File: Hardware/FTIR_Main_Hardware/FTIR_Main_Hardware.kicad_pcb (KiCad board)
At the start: 2 copper layers, 63 parts, among them J1 RJ45_LED_Shielded, Q1 IRF7606PBF, Q2 BSS138, Q3 IRF7606PBF, Q4 IRF7606PBF, Q5 BSS138, Q6 BSS138, U1 Opamp_Dual, U2 D36V28F7, U3 OKI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

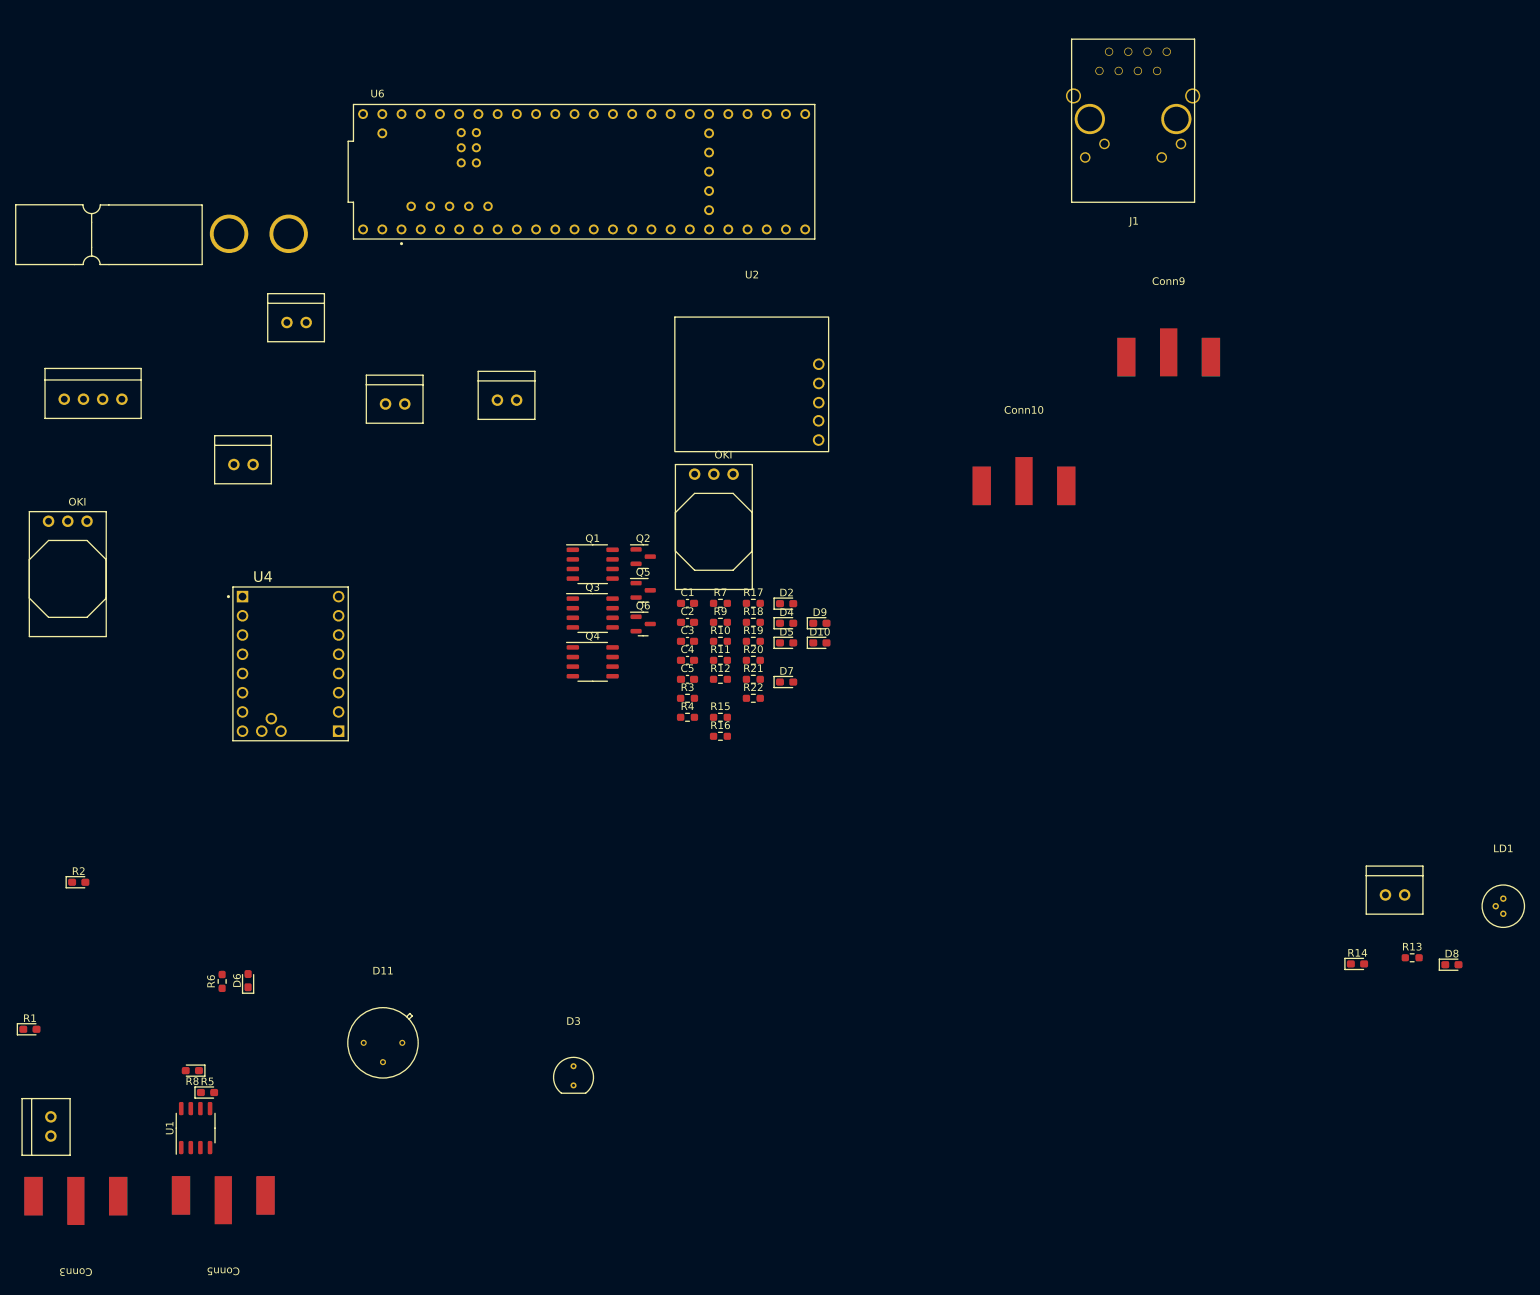
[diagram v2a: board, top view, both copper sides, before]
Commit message: Fixed all custom footprint problems and began boards
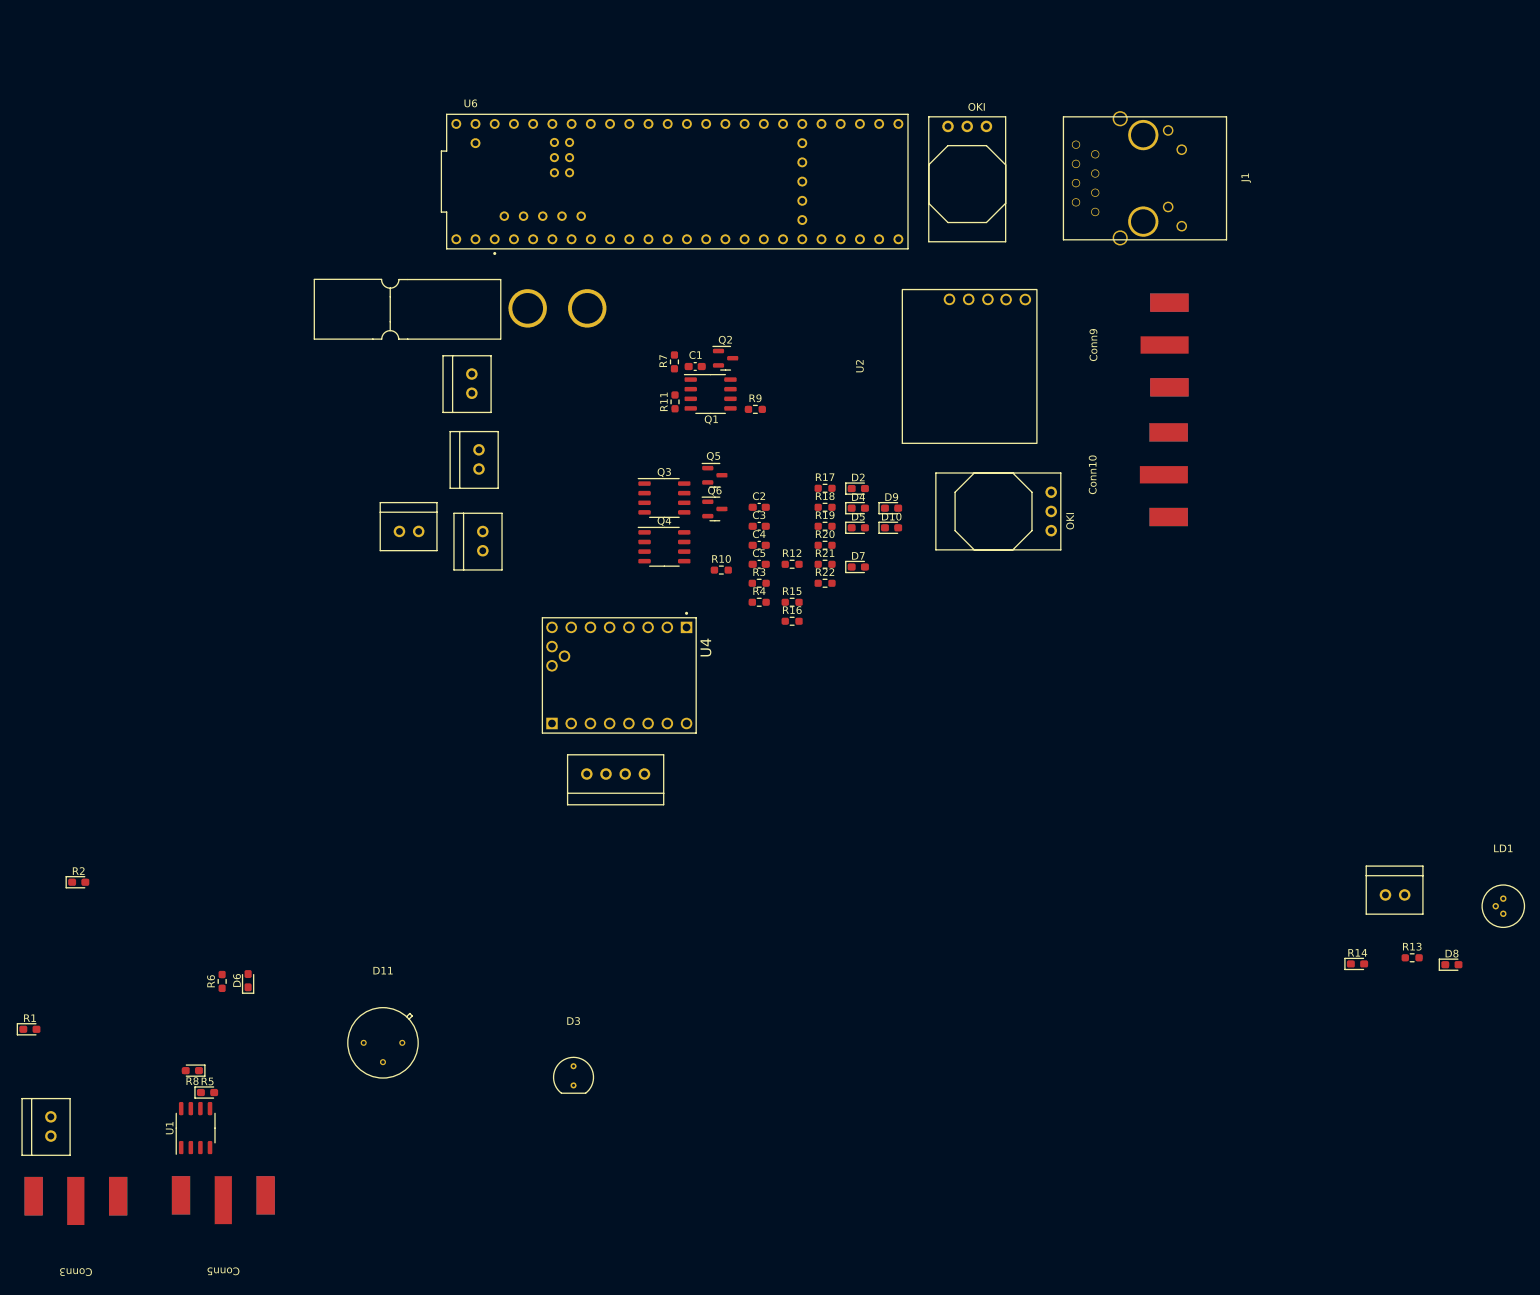
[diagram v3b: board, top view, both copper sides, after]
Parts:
- moved U7 132.5 mm to (194.5, 83.2), turned to -90 degrees
- moved Conn4 91.3 mm to (140.7, 120.5), turned to 180 degrees
- moved U3 56.9 mm to (180.8, 34.9)
- moved U4 43.9 mm to (137.4, 106.9), turned to -90 degrees
- moved Conn1 40.7 mm to (125.3, 58.9)
- moved Conn11 34.8 mm to (119.4, 91.0), turned to 90 degrees
- moved R11 34.7 mm to (144.8, 71.3), turned to 90 degrees
- moved R7 32.5 mm to (144.7, 66.0), turned to -90 degrees
- moved C1 31.3 mm to (147.4, 66.6)
- moved R9 28.5 mm to (155.4, 72.3)
- moved Q2 28.4 mm to (151.5, 65.5)
- moved Q1 27.4 mm to (149.5, 70.3)
- moved Conn6 26.2 mm to (117.9, 70.2), turned to 90 degrees
- moved U2 25.3 mm to (180.3, 66.5), turned to 90 degrees
- moved Conn10 19.2 mm to (210.0, 80.9), turned to 90 degrees
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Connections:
- Conn1 pad 4: (no net) -> +12V
- U2 pad EN: (no net) -> BUCK_EN
- U2 pad GND: (no net) -> GND
- U2 pad VIN: (no net) -> +12V
- U2 pad VOUT: (no net) -> +7.5V
- U4 pad CLK: unconnected-(U4-PadCLK) -> CLK
- U4 pad PDN: unconnected-(U4-PadPDN) -> PDN
- U4 pad UART: GND -> UART
- U6 pad 28: unconnected-(U6-RX7-Pad28) -> CLK
- U6 pad 39: unconnected-(U6-A15-Pad39) -> UART
- U6 pad 40: unconnected-(U6-A16-Pad40) -> PDN

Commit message: Rev1 layout ready for review
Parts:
- added H1: MountingHole, MRDT_Drill_Holes:4_40_Hole_Corner, F.Cu at (108.9, 77.0)
- added H10: MountingHole, MRDT_Drill_Holes:4_40_Hole_Corner, F.Cu at (124.7, 112.1)
- added H11: MountingHole, MRDT_Drill_Holes:4_40_Hole_Corner, F.Cu at (142.1, 94.7)
- added H12: MountingHole, MRDT_Drill_Holes:4_40_Hole_Corner, F.Cu at (142.1, 112.1)
- added H2: MountingHole, MRDT_Drill_Holes:4_40_Hole_Corner, F.Cu at (198.7, 77.0)
- added H3: MountingHole, MRDT_Drill_Holes:4_40_Hole_Corner, F.Cu at (108.9, 37.3)
- added H4: MountingHole, MRDT_Drill_Holes:4_40_Hole_Corner, F.Cu at (198.7, 37.3)
- added H5: MountingHole, MRDT_Drill_Holes:4_40_Hole_Corner, F.Cu at (159.4, 97.1)
- added H6: MountingHole, MRDT_Drill_Holes:4_40_Hole_Corner, F.Cu at (169.4, 94.7)
- added H7: MountingHole, MRDT_Drill_Holes:4_40_Hole_Corner, F.Cu at (124.6, 94.6)
- added H8: MountingHole, MRDT_Drill_Holes:4_40_Hole_Corner, F.Cu at (159.3, 94.7)
- added H9: MountingHole, MRDT_Drill_Holes:4_40_Hole_Corner, F.Cu at (169.4, 97.1)
- Conn1: footprint MRDT_Connectors:Anderson_2_Horizontal_Stacked -> MRDT_Connectors:Square_Anderson_2_H_Stacked
- D11, D3, LD1: moved to B.Cu
- moved D8 101.6 mm to (162.8, 89.5)
- moved LD1 99.2 mm to (164.4, 95.9), turned to 180 degrees
- moved Conn5 95.8 mm to (147.4, 103.4), turned to 90 degrees
- moved R13 93.6 mm to (166.6, 89.5), turned to 180 degrees
- moved U1 92.8 mm to (133.1, 90.2), turned to 0 degrees
- moved R1 92.7 mm to (127.6, 91.2), turned to 180 degrees
- moved R8 91.1 mm to (138.7, 89.2)
- moved R5 90.8 mm to (138.7, 90.9)
- moved Conn3 90.5 mm to (119.3, 103.4), turned to -90 degrees
- moved Conn2 89.1 mm to (134.6, 116.2), turned to 180 degrees
- moved J1 88.9 mm to (132.5, 24.3), turned to 180 degrees
- moved R14 82.7 mm to (168.6, 96.3), turned to 90 degrees
- moved Conn7 81.1 mm to (165.7, 101.1), turned to 180 degrees
- moved R2 77.3 mm to (127.6, 88.1)
- moved U3 76.8 mm to (104.4, 42.0)
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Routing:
- net +5V: track 0.00 -> 172.0 mm, vias 0 -> 6
- net +3V3: track 0.00 -> 148.0 mm, vias 0 -> 8
- net +12V: track 0.00 -> 140.5 mm, vias 0 -> 6
- net MS2_CTRL: track 0.00 -> 105.5 mm, vias 0 -> 3
- net MS1_CTRL: track 0.00 -> 102.5 mm, vias 0 -> 5
- net Net-(Conn6-Pad1): track 0.00 -> 85.9 mm, vias 0 -> 8
- net +7.5V: track 0.00 -> 81.2 mm
- net ETH_LED: track 0.00 -> 75.5 mm, vias 0 -> 3
- net STEP: track 0.00 -> 74.3 mm, vias 0 -> 4
- net DRIVER_EN: track 0.00 -> 73.2 mm, vias 0 -> 2
- net DIR: track 0.00 -> 72.8 mm, vias 0 -> 8
- net R+: track 0.00 -> 69.9 mm, vias 0 -> 2
- net R-: track 0.00 -> 69.6 mm, vias 0 -> 2
- net Net-(Conn12-Pad1): track 0.00 -> 66.3 mm, vias 0 -> 2
- net T-: track 0.00 -> 62.9 mm, vias 0 -> 2
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- added copper zone on B.Cu, net GND
- added copper zone on F.Cu, net GND
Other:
- board outline added: 105.9 x 90.9 mm

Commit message: Delete'd Drew's stuff
Was bad >:(
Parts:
- added D1: Green, LED_SMD:LED_0603_1608Metric_Pad1.05x0.95mm_HandSolder, F.Cu at (234.3, 42.4)
- added R23: 100, Resistor_SMD:R_0603_1608Metric_Pad0.98x0.95mm_HandSolder, F.Cu at (234.3, 45.0)
- Conn1: footprint MRDT_Connectors:Square_Anderson_2_H_Stacked -> MRDT_Connectors:Square_Anderson_2_H_Side_By_Side
- U6: footprint MRDT_Shields:Teensy_4_1 -> MRDT_Shields:Teensy_4_1_Ethernet
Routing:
- net +5V: track 172.0 -> 14.5 mm, vias 6 -> 0
- net +12V: track 140.5 -> 0.00 mm, vias 6 -> 0
- net +3V3: track 148.0 -> 34.8 mm, vias 8 -> 0
- net MS2_CTRL: track 105.5 -> 0.00 mm, vias 3 -> 0
- net MS1_CTRL: track 102.5 -> 0.00 mm, vias 5 -> 0
- net Net-(Conn6-Pad1): track 85.9 -> 0.00 mm, vias 8 -> 0
- net +7.5V: track 81.2 -> 0.00 mm
- net ETH_LED: track 75.5 -> 0.00 mm, vias 3 -> 0
- net STEP: track 74.3 -> 0.00 mm, vias 4 -> 0
- net DRIVER_EN: track 73.2 -> 0.00 mm, vias 2 -> 0
- net DIR: track 72.8 -> 0.00 mm, vias 8 -> 0
- net R+: track 69.9 -> 0.00 mm, vias 2 -> 0
- net R-: track 69.6 -> 0.00 mm, vias 2 -> 0
- net Net-(Conn12-Pad1): track 66.3 -> 0.00 mm, vias 2 -> 0
- net T-: track 62.9 -> 0.00 mm, vias 2 -> 0
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
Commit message: Third time's the charm
Layout try 3
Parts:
- C3, D10, D7, D9, Q1, Q2, Q3, Q4, Q5, Q6, R10, R11, R12, R15, R16, R17, R18, R19, R20, R21, R22, R9: moved to B.Cu
- moved R23 105.2 mm to (134.1, 77.0)
- moved D1 102.5 mm to (137.8, 77.0), turned to 180 degrees
- moved Conn9 93.4 mm to (105.7, 76.1), turned to 90 degrees
- moved J1 90.0 mm to (188.3, 94.9), turned to 90 degrees
- moved Conn10 76.4 mm to (171.6, 108.5), turned to 0 degrees
- moved R9 75.1 mm to (182.8, 44.9), turned to -90 degrees
- moved D7 73.4 mm to (182.8, 48.8), turned to 90 degrees
- moved U6 65.8 mm to (133.3, 101.7), turned to 0 degrees
- moved R3 63.8 mm to (134.0, 72.9), turned to 0 degrees
- moved R20 61.8 mm to (165.4, 45.0), turned to -90 degrees
- moved D2 59.7 mm to (137.8, 72.9), turned to 180 degrees
- moved D10 58.7 mm to (165.4, 48.9), turned to 90 degrees
- moved C2 54.3 mm to (124.6, 91.6)
- moved U4 48.2 mm to (175.9, 78.3), turned to 90 degrees
- moved C1 47.7 mm to (127.3, 81.9), turned to 90 degrees
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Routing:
- removed copper zone on F.Cu, net GND
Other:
- board size 105.9 x 90.9 mm -> 72.3 x 35.1 mm
- board text added: "+12V"
- board text added: "+3.3V"
- board text added: "+5V"
- board text added: "+7.5V"

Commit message: Edge cuts and placing
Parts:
- moved R10 57.2 mm to (128.1, 76.2)
- moved Q1 57.2 mm to (127.1, 71.3)
- moved R11 57.2 mm to (125.1, 77.1)
- moved D7 57.2 mm to (131.0, 73.0)
- moved Q2 57.2 mm to (128.2, 79.4)
- moved R12 57.2 mm to (131.0, 79.4)
- moved R9 57.2 mm to (131.0, 69.2)
- moved C3 40.8 mm to (169.4, 89.2), turned to 180 degrees
- moved R18 27.6 mm to (145.4, 76.8)
- moved Q4 27.6 mm to (147.3, 70.9)
- moved R20 27.6 mm to (151.3, 68.8)
- moved R22 27.6 mm to (151.3, 79.2)
- moved D10 27.6 mm to (151.3, 72.6)
- moved R16 27.6 mm to (148.1, 75.8)
- moved Q6 27.6 mm to (148.1, 78.9)
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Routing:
- added copper zone on F.Cu, net GND
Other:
- board size 72.3 x 35.1 mm -> 85.9 x 99.3 mm

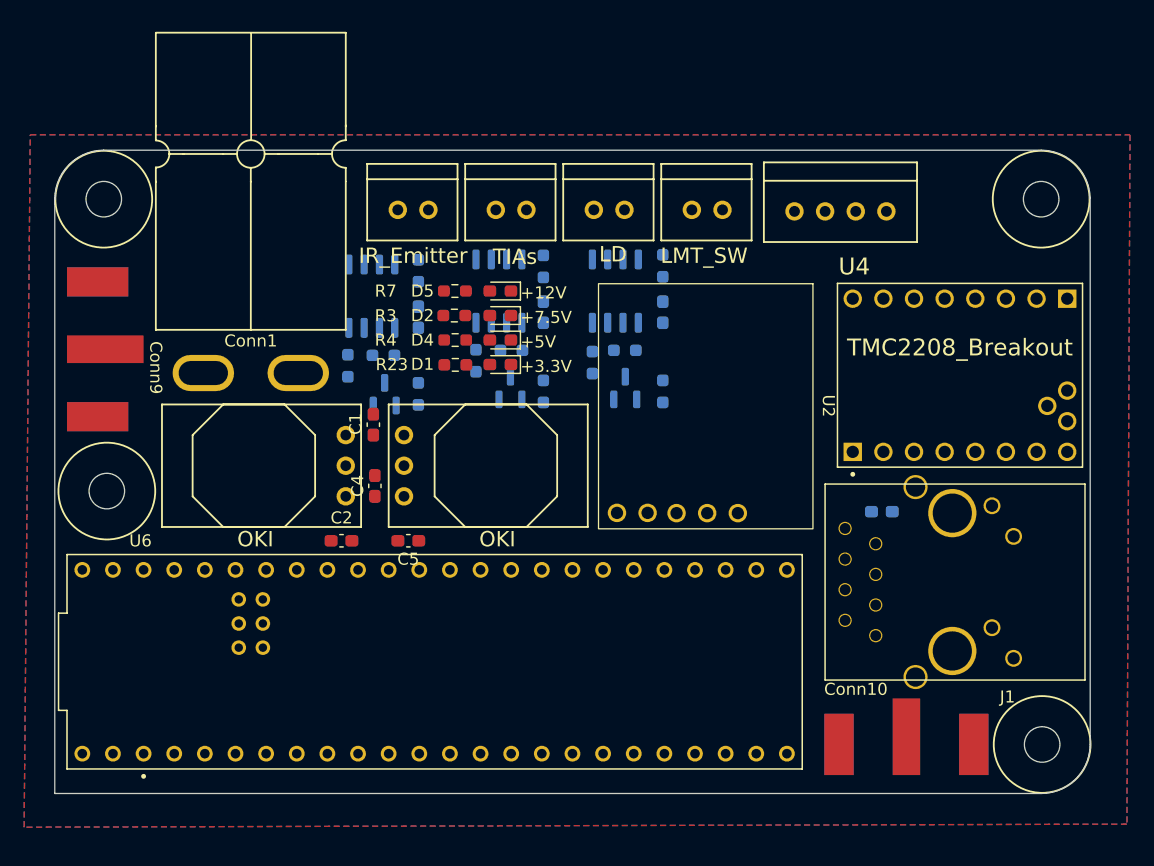
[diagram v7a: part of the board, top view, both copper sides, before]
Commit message: Fixed edge cut dimensions
From center of hole mounts:
3060 mils
1770 mills
From the top left to the center left:
980 mils
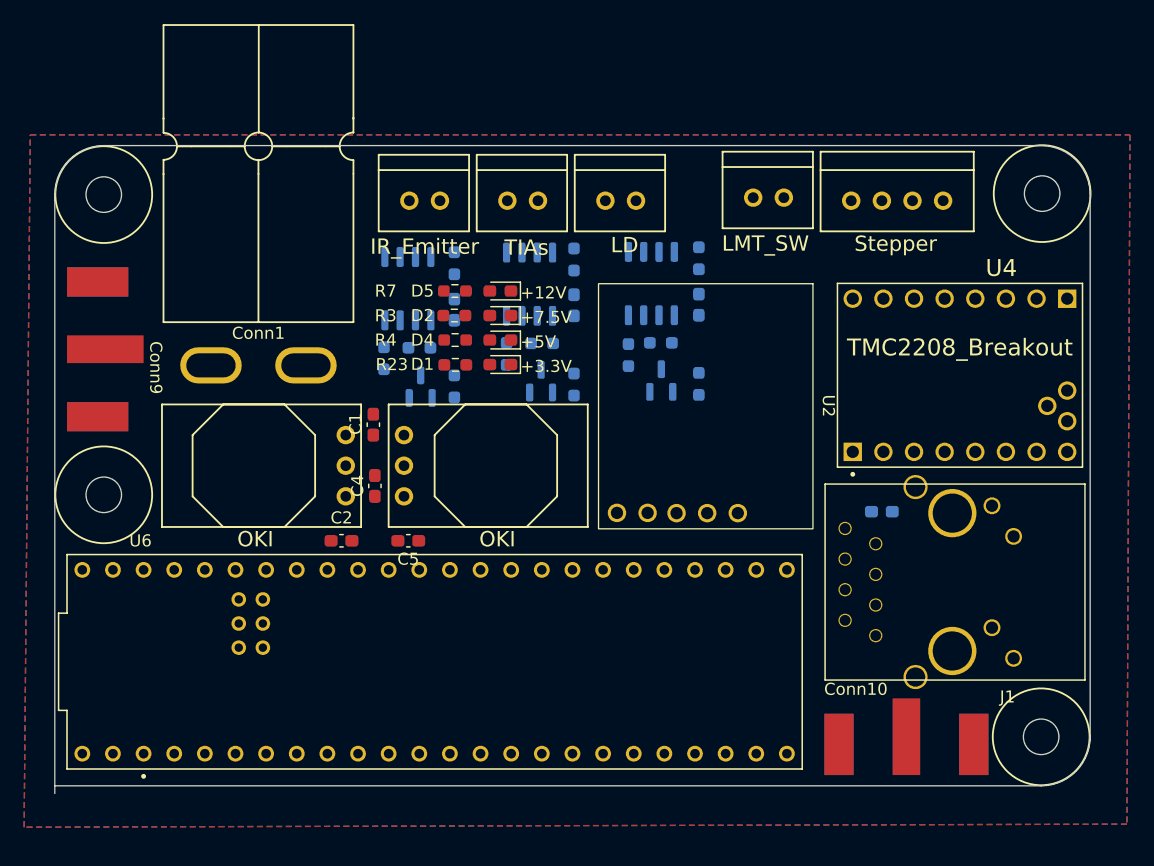
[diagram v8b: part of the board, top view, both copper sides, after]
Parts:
- moved Conn8 5.18 mm to (158.8, 63.1)
- moved Conn4 4.79 mm to (166.9, 63.4)
- moved R10 3.05 mm to (131.1, 75.6)
- moved Q1 3.05 mm to (130.1, 70.7)
- moved R11 3.05 mm to (128.1, 76.4)
- moved D10 3.05 mm to (154.2, 72.0)
- moved D7 3.05 mm to (134.0, 72.4)
- moved Q2 3.05 mm to (131.2, 78.8)
- moved Q4 3.05 mm to (150.3, 70.2)
- moved R12 3.05 mm to (134.0, 78.8)
- moved R16 3.05 mm to (151.1, 75.2)
- moved R18 3.05 mm to (148.4, 76.2)
- moved R20 3.05 mm to (154.2, 68.1)
- moved R22 3.05 mm to (154.2, 78.6)
- moved R9 3.05 mm to (134.0, 68.6)
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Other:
- board size 85.9 x 99.3 mm -> 85.9 x 99.7 mm
- board text added: "Stepper"
